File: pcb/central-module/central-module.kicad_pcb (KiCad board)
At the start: 2 copper layers, 100 x 100 mm, 21 parts, among them J1 Conn_01x10_Pin, J2 Screw_Terminal_01x04, J3 Conn_01x04_Pin, J4 Screw_Terminal_01x03, J5 Screw_Terminal_01x04, U1 ESP32_DEVCITV1, U2 74HC245

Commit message: improvements first soldering
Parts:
- moved F4 30.4 mm to (108.8, 119.3), turned to 90 degrees
- moved F3 20.5 mm to (129.3, 88.3)
- moved F2 0.40 mm to (109.7, 75.0)
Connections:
- net Net-(J2-Pin_2) renamed /T_BRIDGE
- net Net-(J2-Pin_4) renamed /24VAC_P_UF
- net Net-(J4-Pin_3) renamed /+24V_UF
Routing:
- net Net-(J4-Pin_2): track 51.0 -> 75.8 mm
- net /+24V_UF: track 45.6 -> 65.5 mm
- net +24V: track 61.2 -> 42.1 mm
- net +5V: track 147.8 -> 157.4 mm
- net /24VAC_P_UF: track 101.1 -> 99.7 mm
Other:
- board text added: "Splitflap 'ABC' Central Unit v1.1"

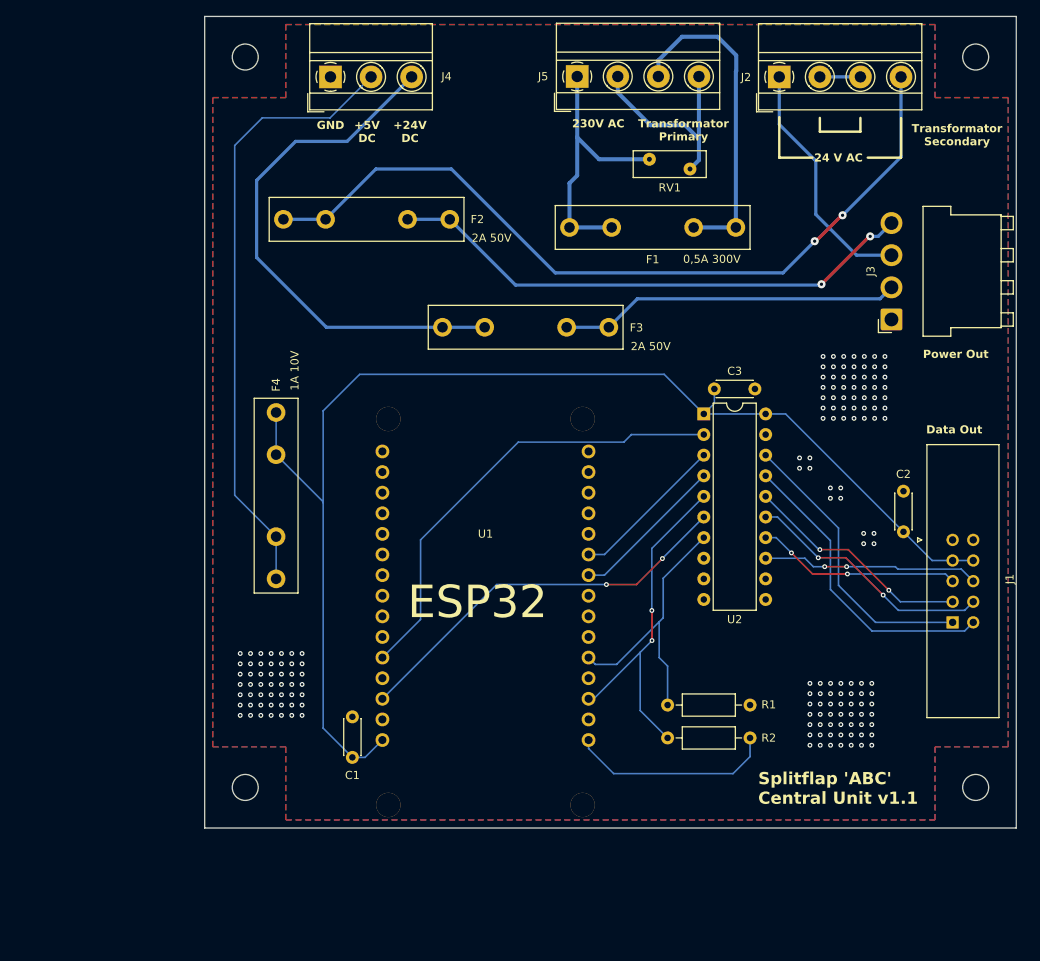
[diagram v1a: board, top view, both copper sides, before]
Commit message: first version firmware, rounded corners
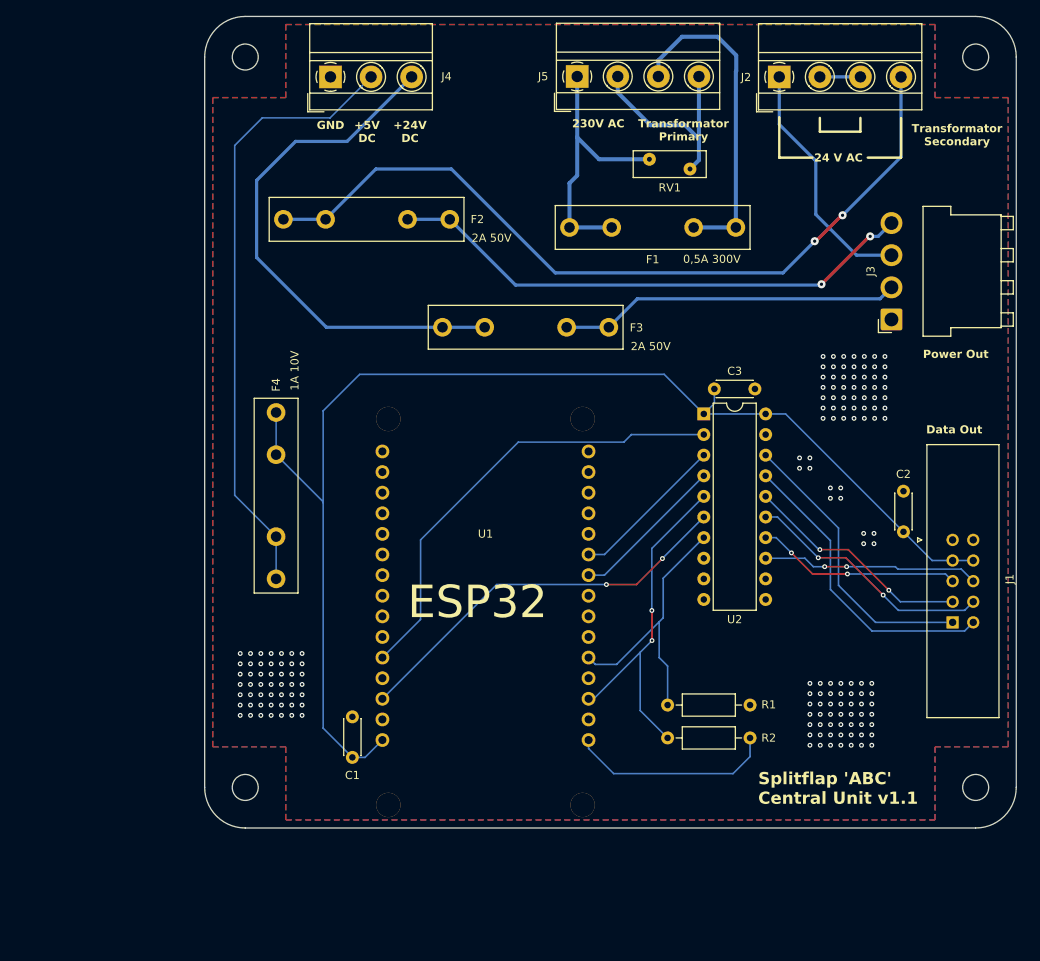
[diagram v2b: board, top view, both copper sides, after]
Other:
- outline, holes or cut-outs redrawn
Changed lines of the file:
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@@
 		(layer "F.SilkS")
 	)
-	(gr_rect
-		(start 100 50)
-		(end 200 150)
+	(gr_line
+		(start 195 150)
+		(end 105 150)
 		(stroke
 			(width 0.05)
 			(type default)
 		)
-		(fill none)
 		(layer "Edge.Cuts")
 	)
+	(gr_line
+		(start 200 55)
+		(end 200 145)
+		(stroke
+			(width 0.05)
+			(type default)
+		)
+		(layer "Edge.Cuts")
+	)
+	(gr_arc
+		(start 105 150)
+		(mid 101.464466 148.535534)
+		(end 100 145)
+		(stroke
+			(width 0.05)
+			(type default)
+		)
+		(layer "Edge.Cuts")
+	)
+	(gr_arc
+		(start 200 145)
+		(mid 198.535534 148.535534)
+		(end 195 150)
+		(stroke
+			(width 0.05)
+			(type default)
+		)
+		(layer "Edge.Cuts")
+	)
+	(gr_line
+		(start 105 50)
+		(end 195 50)
+		(stroke
+			(width 0.05)
+			(type default)
+		)
+		(layer "Edge.Cuts")
+	)
+	(gr_arc
+		(start 100 55)
+		(mid 101.464466 51.464466)
+		(end 105 50)
+		(stroke
+			(width 0.05)
+			(type default)
+		)
+		(layer "Edge.Cuts")
+	)
+	(gr_line
+		(start 100 145)
+		(end 100 55)
+		(stroke
+			(width 0.05)
+			(type default)
+		)
+		(layer "Edge.Cuts")
+	)
+	(gr_arc
+		(start 195 50)
+		(mid 198.535534 51.464466)
+		(end 200 55)
+		(stroke
+			(width 0.05)
+			(type default)
+		)
+		(layer "Edge.Cuts")
+	)

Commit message: beschriftungen sicherungen
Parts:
- F1: value 0,5A 300V -> 0,5A 250V
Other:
- board text added: "FUSE 24 VAC"
- board text added: "FUSE 24 VDC"
- board text added: "FUSE 5 VDC"
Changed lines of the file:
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@@
 			)
 		)
-		(property "Value" "0,5A 300V"
+		(property "Value" "0,5A 250V"
 			(at 2.95 -3.9 0)
 			(unlocked yes)
@@
 		)
 	)
+	(gr_text "FUSE 5 VDC"
+		(at 104.6 123.2 0)
+		(layer "F.SilkS")
+		(effects
+			(font
+				(size 1 1)
+				(thickness 0.15)
+			)
+			(justify left bottom)
+		)
+	)
 	(gr_text "Data Out"
 		(at 188.9 101.5 0)
@@
 		)
 	)
+	(gr_text "FUSE 24 VDC"
+		(at 134.5 93.3 0)
+		(layer "F.SilkS")
+		(effects
+			(font
+				(size 1 1)
+				(thickness 0.15)
+			)
+			(justify left bottom)
+		)
+	)
 	(gr_text "230V AC"
 		(at 148.5 63.790056 0)
@@
 		)
 	)
+	(gr_text "FUSE 24 VAC"
+		(at 115.1 80 0)
+		(layer "F.SilkS")
+		(effects
+			(font
+				(size 1 1)
+				(thickness 0.15)
+			)
+			(justify left bottom)
+		)
+	)
 	(gr_text "ESP32 "
 		(at 125 124.5 0)
@@
 		(min_thickness 0.25)
 		(filled_areas_thickness no)
-		(fill yes
+		(fill
 			(thermal_gap 0.5)
 			(thermal_bridge_width 0.5)

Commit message: many improvements
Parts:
- added Q1: IRF3205, Package_TO_SOT_THT:TO-220-3_Vertical, F.Cu at (79.4, 109.6)
- added R3: 10K, Resistor_THT:R_Axial_DIN0207_L6.3mm_D2.5mm_P10.16mm_Horizontal, F.Cu at (77.8, 100.8)
- added R4: 10K, Resistor_THT:R_Axial_DIN0207_L6.3mm_D2.5mm_P10.16mm_Horizontal, F.Cu at (165.1, 154.9)
- added R5: 10K, Resistor_THT:R_Axial_DIN0207_L6.3mm_D2.5mm_P10.16mm_Horizontal, F.Cu at (165.3, 163.0)
- F1: value 0,5A 250V -> 0,5A 300V
- R1, R2: value 4K7 -> 10K
- RV1: footprint Varistor:RV_Disc_D9mm_W3.3mm_P5mm -> Varistor:RV_Disc_D15.5mm_W3.9mm_P7.5mm
- moved F2 63.0 mm to (172.2, 67.4)
- moved F3 31.9 mm to (105.6, 66.9), turned to -90 degrees
- moved RV1 9.24 mm to (150.6, 67.9), turned to 0 degrees
- moved J5 4.90 mm to (141.0, 57.4)
- moved F1 4.90 mm to (160.6, 76.0)
- moved F4 3.27 mm to (105.6, 118.7)
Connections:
- J3 pad 1: GND -> Net-(J3-Pin_1)
- RV1 pad 2: /P -> /P_FUSED
- U1 pad 27: unconnected-(U1-D2-Pad27) -> DC_PWR_3
- U2 pad 11: unconnected-(U2-B7-Pad11) -> Net-(U2-B7)
- U2 pad 12: unconnected-(U2-B6-Pad12) -> DC_PWR
- U2 pad 8: unconnected-(U2-A6-Pad8) -> DC_PWR_3
- U2 pad 9: unconnected-(U2-A7-Pad9) -> Net-(U2-A7)
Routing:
- net /24VAC_P_UF: track 99.7 -> 20.2 mm, vias 2 -> 0
- net Net-(J4-Pin_2): track 75.8 -> 0.00 mm
- net /24VAC_P: track 66.1 -> 14.5 mm, vias 2 -> 0
- net +24V: track 42.1 -> 85.9 mm
- net /+24V_UF: track 65.5 -> 29.0 mm
- net +5V: track 157.4 -> 143.9 mm
- net /P: track 34.2 -> 24.2 mm
- net /P_FUSED: track 40.2 -> 48.1 mm
- net /24VAC_N: track 30.2 -> 35.6 mm
- net /N: track 26.2 -> 25.1 mm
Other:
- board text added: "Fallblatt Adtranz 'ABC' Central Unit v1.1"
- board text removed: "Splitflap 'ABC' Central Unit v1.1"

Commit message: graytable, both pcbs
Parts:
- added R6: 4K7, Resistor_THT:R_Axial_DIN0207_L6.3mm_D2.5mm_P10.16mm_Horizontal, F.Cu at (151.6, 87.6)
- moved Q1 89.8 mm to (167.0, 89.7)
- moved R3 84.5 mm to (161.8, 91.2), turned to 180 degrees
- moved R5 35.1 mm to (158.9, 128.5)
- moved R4 23.2 mm to (158.9, 132.5)
- moved R1 1.80 mm to (157.0, 136.7)
- moved R2 1.80 mm to (157.0, 140.7)
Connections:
- Q1 pad 1: DC_PWR -> Net-(Q1-G)
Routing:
- net Net-(J4-Pin_2): track 0.00 -> 67.4 mm, vias 0 -> 2
- net DC_PWR: track 0.00 -> 47.3 mm, vias 0 -> 1
- net +5V: track 143.9 -> 166.1 mm
- net Net-(J3-Pin_1): track 0.00 -> 16.7 mm
- net Net-(U2-A7): track 0.00 -> 15.6 mm
- net Net-(U2-B7): track 0.00 -> 14.3 mm
- net Net-(Q1-G): track 0.00 -> 6.09 mm
- net SHIFT_OUTPUT_ENABLE_3: track 43.2 -> 45.7 mm
- net SPIN_ENABLE_3: track 34.6 -> 36.4 mm
- net +3.3V: track 25.4 -> 24.1 mm
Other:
- board text added: "N"
- board text added: "P"

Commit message: fuses
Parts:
- F1: value 0,5A 300V -> 1A 300V
- F2: value 2A 50V -> 5A 50V
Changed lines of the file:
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@@
 			)
 		)
-		(property "Value" "0,5A 300V"
+		(property "Value" "1A 300V"
 			(at 2.95 -3.9 0)
 			(unlocked yes)
@@
 			)
 		)
-		(property "Value" "2A 50V"
+		(property "Value" "5A 50V"
 			(at 19.55 4 0)
 			(unlocked yes)
@@
 		(tags "Resistor Axial_DIN0207 series Axial Horizontal pin pitch 10.16mm 0.25W = 1/4W length 6.3mm diameter 2.5mm")
 		(property "Reference" "R3"
-			(at 12.88 0 360)
+			(at 12.88 0 0)
 			(layer "F.SilkS")
 			(effects
@@
 		)
 		(property "Value" "10K"
-			(at 5.08 2.37 360)
+			(at 5.08 2.37 0)
 			(layer "F.Fab")
 			(effects
@@
 		)
 		(fp_text user "${REFERENCE}"
-			(at 5.08 0 360)
+			(at 5.08 0 0)
 			(layer "F.Fab")
 			(effects

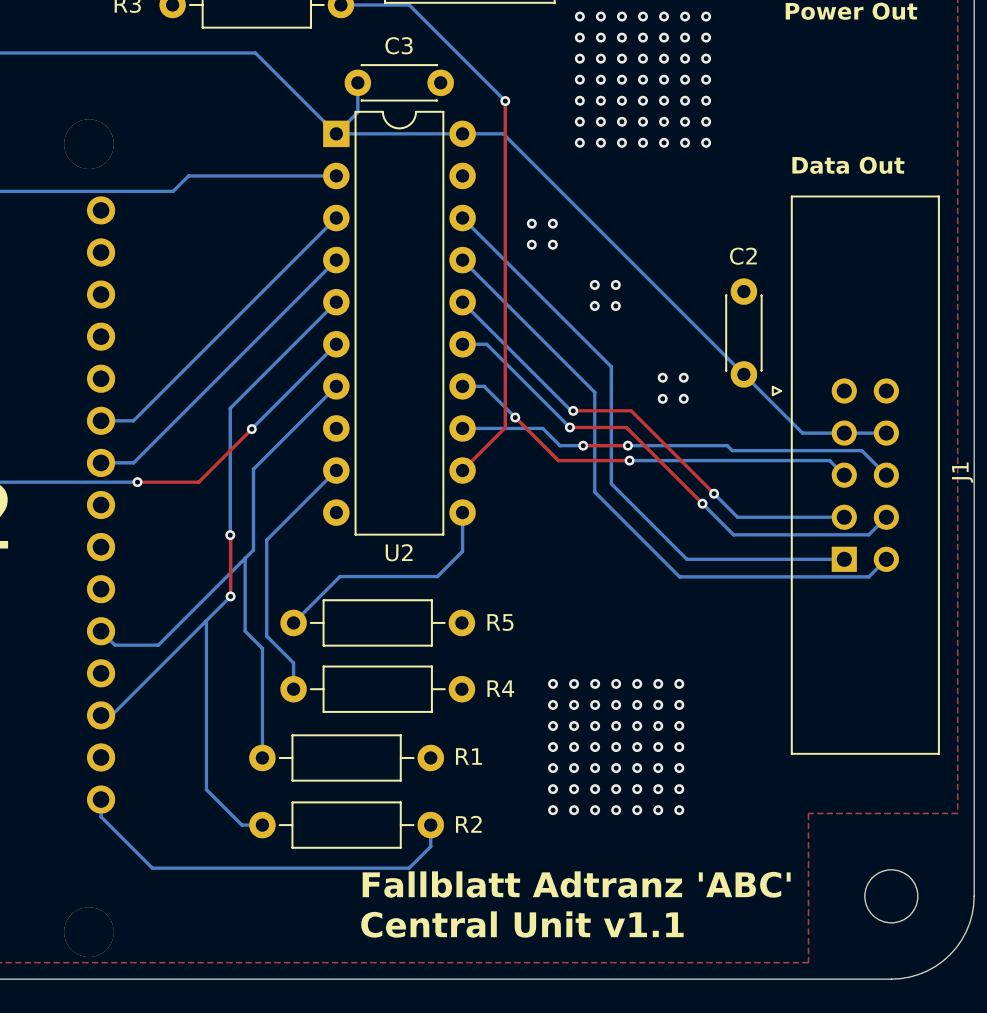
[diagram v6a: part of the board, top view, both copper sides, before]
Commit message: 14 modules, central pcb serial termination
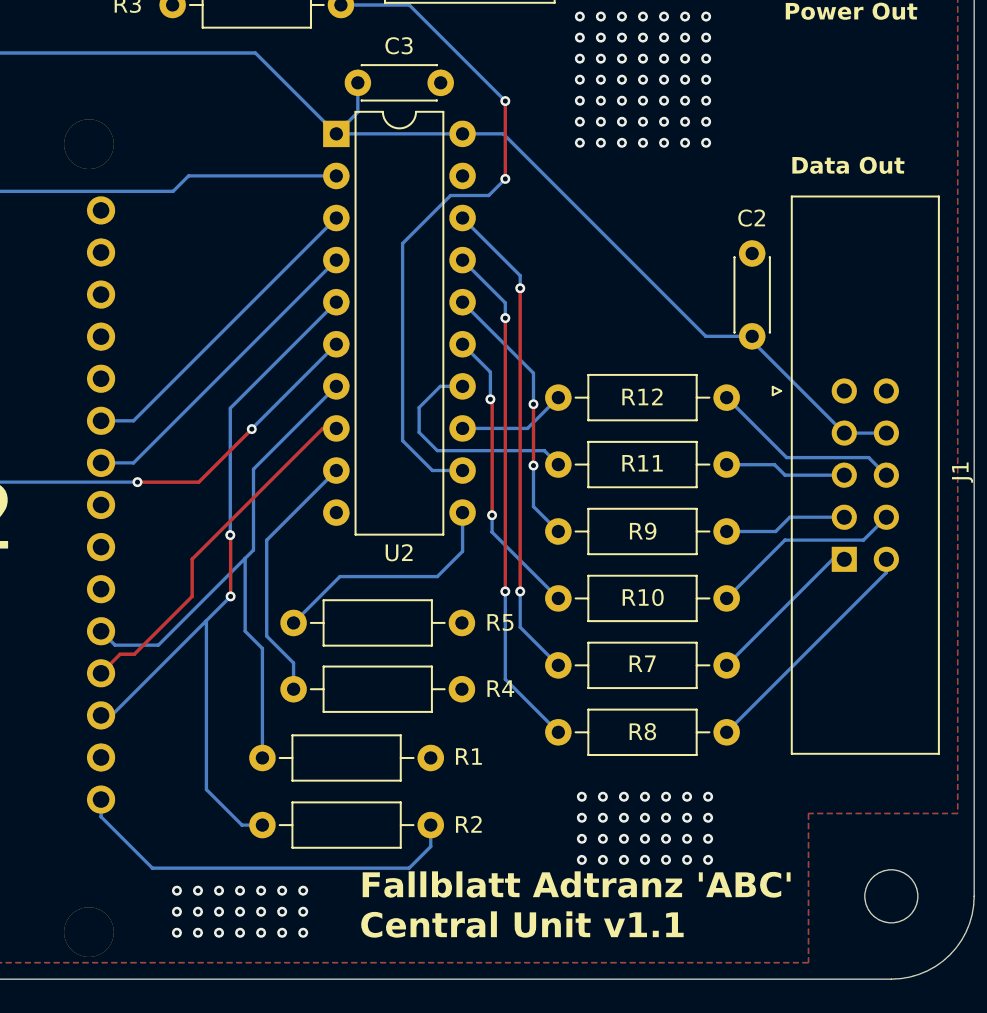
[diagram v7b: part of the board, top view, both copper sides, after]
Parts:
- added R10: 47, Resistor_THT:R_Axial_DIN0207_L6.3mm_D2.5mm_P10.16mm_Horizontal, F.Cu at (185.1, 127.0)
- added R11: ??, Resistor_THT:R_Axial_DIN0207_L6.3mm_D2.5mm_P10.16mm_Horizontal, F.Cu at (185.1, 118.9)
- added R12: 47, Resistor_THT:R_Axial_DIN0207_L6.3mm_D2.5mm_P10.16mm_Horizontal, F.Cu at (185.1, 114.9)
- added R7: 47, Resistor_THT:R_Axial_DIN0207_L6.3mm_D2.5mm_P10.16mm_Horizontal, F.Cu at (185.1, 131.1)
- added R8: 47, Resistor_THT:R_Axial_DIN0207_L6.3mm_D2.5mm_P10.16mm_Horizontal, F.Cu at (185.1, 135.1)
- added R9: 47, Resistor_THT:R_Axial_DIN0207_L6.3mm_D2.5mm_P10.16mm_Horizontal, F.Cu at (185.1, 123.0)
- moved C2 2.35 mm to (186.6, 106.2)
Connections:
- J1 pad 1: SHIFT_CLOCK -> Net-(J1-Pin_1)
- J1 pad 2: SHIFT_CLEAR -> Net-(J1-Pin_2)
- J1 pad 3: SHIFT_LATCH -> Net-(J1-Pin_3)
- J1 pad 4: SHIFT_OUTPUT_ENABLE -> Net-(J1-Pin_4)
- J1 pad 5: DATA_OUT -> Net-(J1-Pin_5)
- J1 pad 6: SPIN_ENABLE -> Net-(J1-Pin_6)
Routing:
- net DC_PWR_3: track 0.00 -> 21.6 mm
- net SPIN_ENABLE: track 26.7 -> 6.55 mm, vias 2 -> 0
- net Net-(J1-Pin_2): track 0.00 -> 14.4 mm
- net SHIFT_OUTPUT_ENABLE: track 30.8 -> 17.7 mm
- net SHIFT_LATCH: track 28.4 -> 16.2 mm
- net Net-(J1-Pin_4): track 0.00 -> 11.7 mm
- net Net-(J1-Pin_6): track 0.00 -> 11.6 mm
- net DATA_OUT: track 25.3 -> 13.9 mm, vias 2 -> 0
- net Net-(J1-Pin_1): track 0.00 -> 9.75 mm
- net Net-(J1-Pin_3): track 0.00 -> 7.71 mm
- net Net-(J1-Pin_5): track 0.00 -> 7.36 mm
- net SHIFT_CLEAR: track 37.5 -> 30.9 mm, vias 0 -> 2
- net SHIFT_CLOCK: track 35.7 -> 29.4 mm, vias 0 -> 2
- net DC_PWR: track 47.3 -> 52.7 mm, vias 1 -> 2
- net GND: vias 159 -> 147
